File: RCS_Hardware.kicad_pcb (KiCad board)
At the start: 2 copper layers, 50.8 x 50 mm, 54 parts, among them J1 SWD, J2 TYPE-C-31-M-12, J3 JST BATT, J4 3V3, J5 GND, J6 Solenoids, J7 Ext Sesnor, U1 STM32F401CCU6, U2 AMS1117-3.3, U3 BMP280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

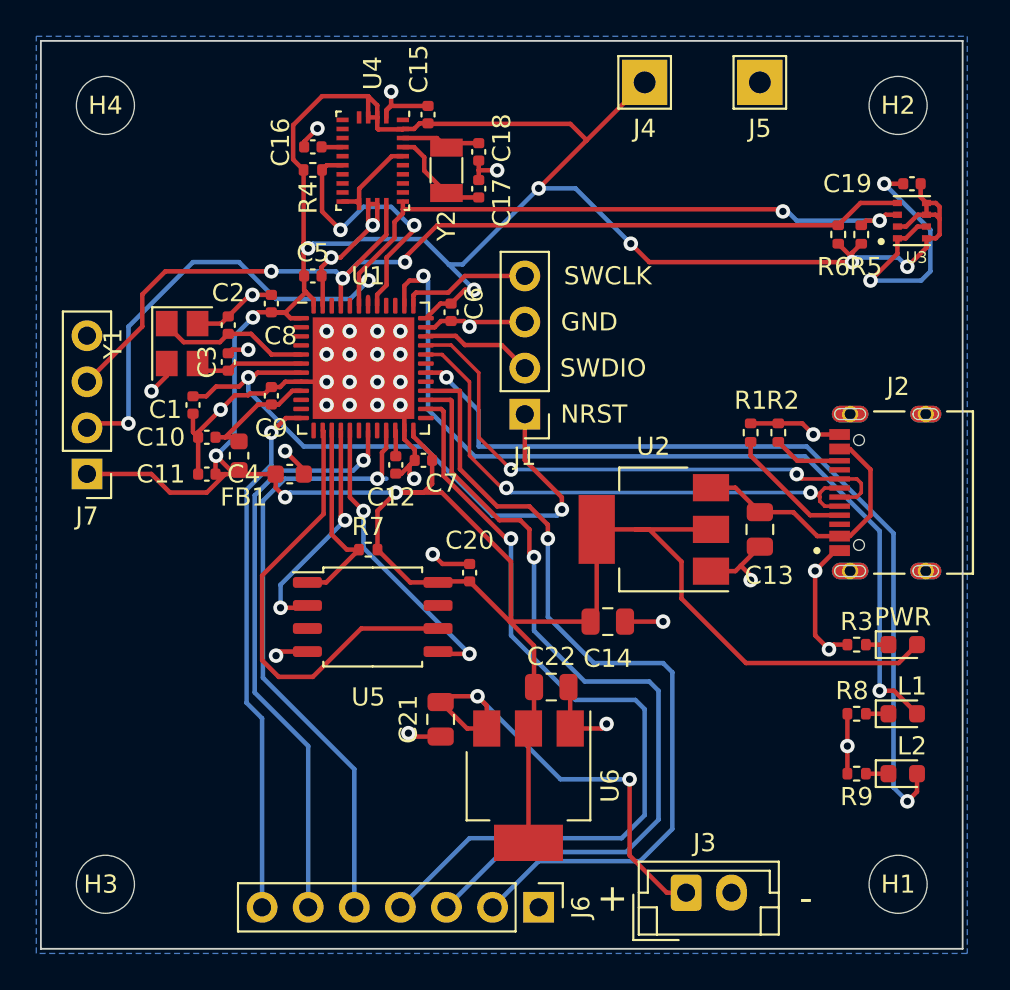
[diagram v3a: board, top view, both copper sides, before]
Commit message: created symbol and footprint for differential driver added schema for diff driver layed out diff driver and connector updated render
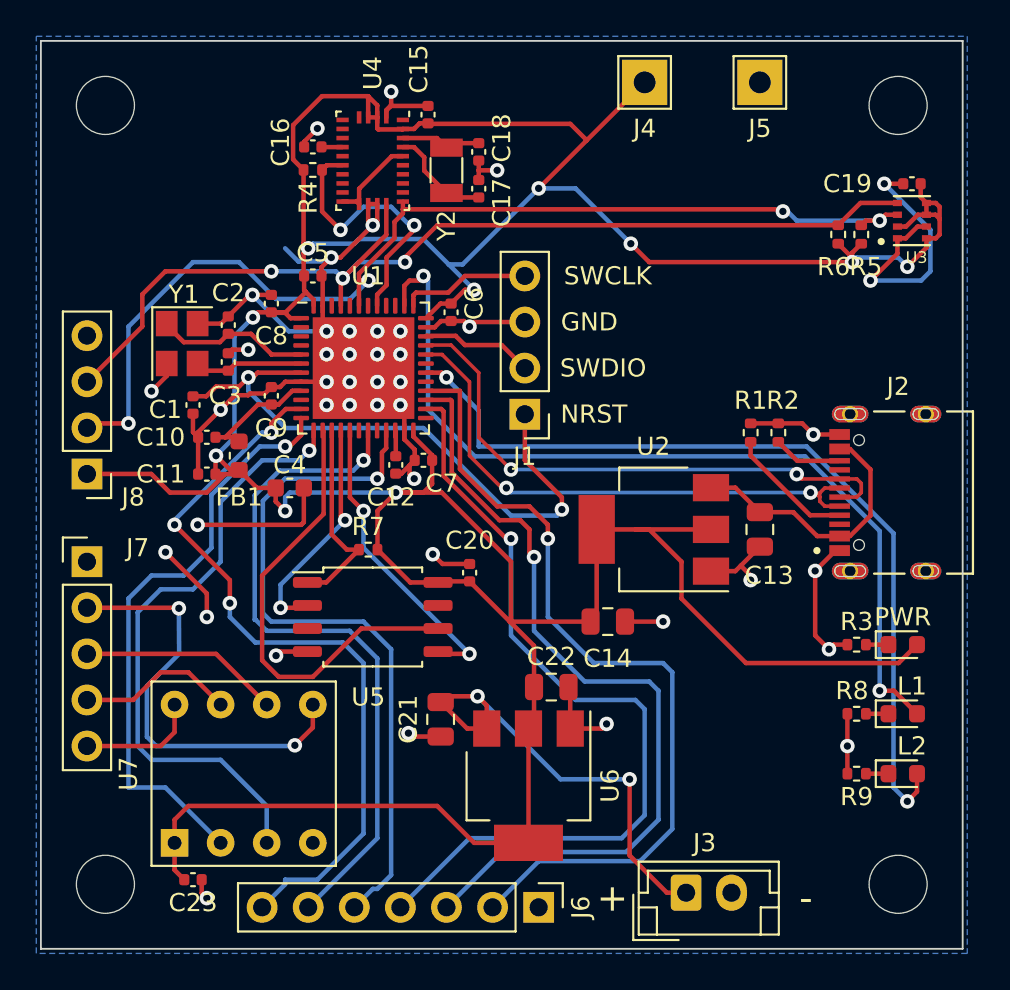
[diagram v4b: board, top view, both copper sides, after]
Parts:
- added C23: 100nF, Capacitor_SMD:C_0402_1005Metric, F.Cu at (119.6, 120.7)
- added J8: Conn_01x05_Male, Connector_PinHeader_2.54mm:PinHeader_1x05_P2.54mm_Vertical, F.Cu at (113.8, 103.1)
- added U7: LT1690N8, LTC1690N8:LTC1690N8, F.Cu at (122.4, 114.8)
- moved C4 0.76 mm to (125.0, 99.1)
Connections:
- U1 pad 11: unconnected-(U1-Pad11) -> /S1
- U1 pad 12: /S1 -> /RX
- U1 pad 13: unconnected-(U1-Pad13) -> /TX
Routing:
- net /TX: track 0.00 -> 34.2 mm, vias 0 -> 1
- net /RX: track 0.00 -> 32.7 mm, vias 0 -> 1
- net +3.3V: track 208.9 -> 234.1 mm
- net Net-(U7-Pad5): track 0.00 -> 23.9 mm, vias 0 -> 2
- net GND: track 103.5 -> 126.7 mm, vias 40 -> 43
- net /S1: track 29.1 -> 41.6 mm, vias 1 -> 3
- net Net-(U7-Pad6): track 0.00 -> 11.1 mm
- net Net-(U7-Pad7): track 0.00 -> 8.73 mm
- net Net-(U7-Pad8): track 0.00 -> 6.67 mm
- net /S2: track 32.5 -> 38.3 mm
- net /S3: track 34.7 -> 39.0 mm
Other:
- board text removed: "ACC2"
